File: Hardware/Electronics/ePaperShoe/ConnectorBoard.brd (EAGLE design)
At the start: 19.3 x 19.2 mm, 3 parts, among them X1 FH12-26S-0.5SH, X2 FH12-26S-0.5SH

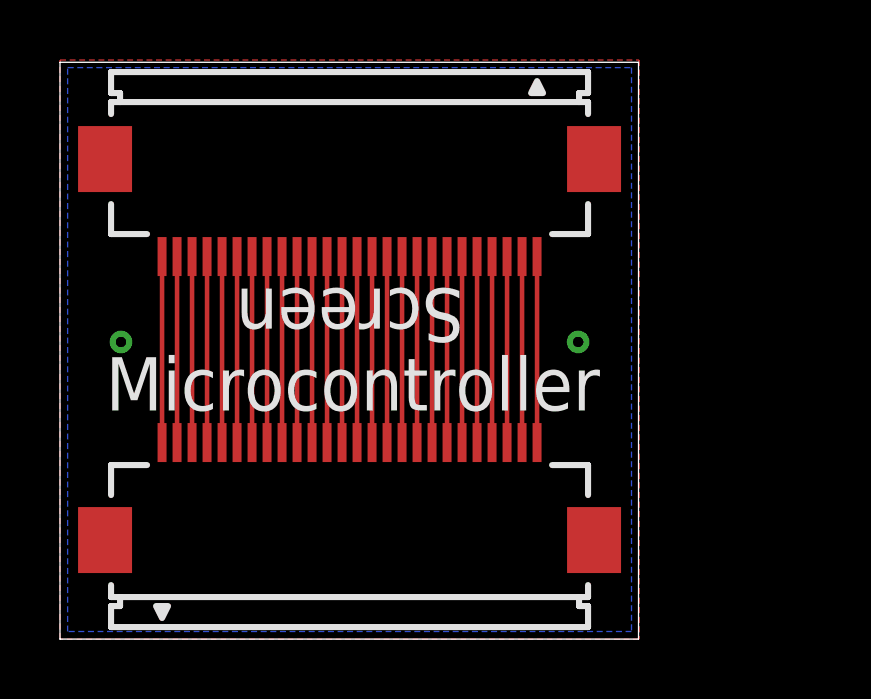
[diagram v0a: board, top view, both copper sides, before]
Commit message: Designed new screen board and made minor changes to the connector board
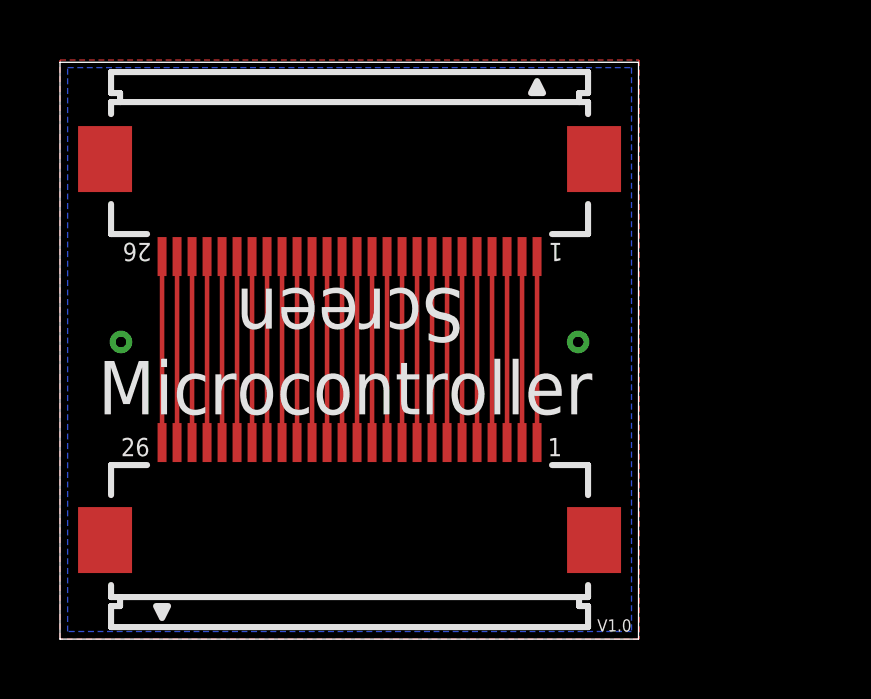
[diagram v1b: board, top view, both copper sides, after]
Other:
- board text added: "1"
- board text added: "26"
- board text added: "V1.0"
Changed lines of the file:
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@@
 <setting verticaltext="up"/>
 </settings>
-<grid distance="10" unitdist="mil" unit="mil" style="lines" multiple="1" display="no" altdistance="5" altunitdist="mil" altunit="mil"/>
+<grid distance="5" unitdist="mil" unit="mil" style="lines" multiple="1" display="no" altdistance="5" altunitdist="mil" altunit="mil"/>
 <layers>
 <layer number="1" name="Top" color="4" fill="1" visible="yes" active="yes"/>
@@
 <wire x1="19.792" y1="19.736" x2="0.508" y2="19.736" width="0" layer="20"/>
 <wire x1="0.508" y1="19.736" x2="0.508" y2="0.508" width="0" layer="20"/>
-<text x="18.034" y="2.794" size="1.778" layer="22" rot="MR0">Microcontroller</text>
-<text x="2.032" y="8.128" size="1.778" layer="21">Microcontroller</text>
+<text x="18.542" y="3.81" size="1.778" layer="22" rot="MR0" align="center-left">Microcontroller</text>
+<text x="1.778" y="8.89" size="1.778" layer="21" align="center-left">Microcontroller</text>
 <text x="13.97" y="12.192" size="1.778" layer="21" rot="SR180">Screen</text>
 <text x="6.35" y="17.526" size="1.778" layer="22" rot="SMR180">Screen</text>
-<text x="1.016" y="15.24" size="0.4064" layer="22" rot="SR270">Made for Bioworld ePaper Screen Project</text>
-<text x="19.558" y="8.636" size="0.4064" layer="22" rot="SR90">Michael Currie</text>
+<text x="19.558" y="19.304" size="0.4064" layer="22" rot="SMR270">Made for Bioworld ePaper Screen Project</text>
+<text x="19.558" y="4.572" size="0.4064" layer="22" rot="SMR270">Michael Currie</text>
+<text x="18.415" y="0.762" size="0.4064" layer="21" rot="SR0">V1.0</text>
+<text x="16.764" y="6.604" size="0.6096" layer="21">1</text>
+<text x="17.272" y="13.716" size="0.6096" layer="21" rot="SR180">1</text>
+<text x="3.556" y="13.716" size="0.6096" layer="21" rot="SR180">26</text>
+<text x="2.54" y="6.604" size="0.6096" layer="21">26</text>
 </plain>
 <attributes>
@@
 <contactref element="X1" pad="26"/>
 <contactref element="X2" pad="1"/>
-<wire x1="16.41" y1="7.06" x2="16.41" y2="13.26" width="0.1524" layer="1"/>
-</signal>
-<signal name="N$2">
-<contactref element="X1" pad="25"/>
-<contactref element="X2" pad="2"/>
-<wire x1="15.91" y1="7.06" x2="15.91" y2="13.26" width="0.1524" layer="1"/>
-</signal>
-<signal name="N$3">
-<contactref element="X1" pad="24"/>
-<contactref element="X2" pad="3"/>
-<wire x1="15.41" y1="7.06" x2="15.41" y2="13.26" width="0.1524" layer="1"/>
-</signal>
-<signal name="N$4">
-<contactref element="X1" pad="23"/>
-<contactref element="X2" pad="4"/>
-<wire x1="14.91" y1="7.06" x2="14.91" y2="13.26" width="0.1524" layer="1"/>
+<wire x1="16.41" y1="13.26" x2="16.41" y2="7.06" width="0.1524" layer="1"/>
 </signal>
 <signal name="N$5">
@@
 <wire x1="13.41" y1="7.06" x2="13.41" y2="13.26" width="0.1524" layer="1"/>
 </signal>
-<signal name="N$8">
-<contactref element="X1" pad="19"/>
-<contactref element="X2" pad="8"/>
-<wire x1="12.91" y1="7.06" x2="12.91" y2="13.26" width="0.1524" layer="1"/>
-</signal>
-<signal name="N$9">
-<contactref element="X1" pad="18"/>
-<contactref element="X2" pad="9"/>
-<wire x1="12.41" y1="7.06" x2="12.41" y2="13.26" width="0.1524" layer="1"/>
-</signal>
 <signal name="N$10">
 <contactref element="X1" pad="17"/>
@@
 <wire x1="7.91" y1="7.06" x2="7.91" y2="13.26" width="0.1524" layer="1"/>
 </signal>
-<signal name="N$19">
-<contactref element="X1" pad="8"/>
-<contactref element="X2" pad="19"/>
-<wire x1="7.41" y1="7.06" x2="7.41" y2="13.26" width="0.1524" layer="1"/>
-</signal>
 <signal name="N$20">
 <contactref element="X1" pad="7"/>
@@
 <contactref element="X2" pad="22"/>
 <wire x1="5.91" y1="7.06" x2="5.91" y2="13.26" width="0.1524" layer="1"/>
-</signal>
-<signal name="N$23">
-<contactref element="X1" pad="4"/>
-<contactref element="X2" pad="23"/>
-<wire x1="5.41" y1="7.06" x2="5.41" y2="13.26" width="0.1524" layer="1"/>
-</signal>
-<signal name="N$24">
-<contactref element="X1" pad="3"/>
-<contactref element="X2" pad="24"/>
-<wire x1="4.91" y1="7.06" x2="4.91" y2="13.26" width="0.1524" layer="1"/>
-</signal>
-<signal name="N$25">
-<contactref element="X1" pad="2"/>
-<contactref element="X2" pad="25"/>
-<wire x1="4.41" y1="7.06" x2="4.41" y2="13.26" width="0.1524" layer="1"/>
 </signal>
 <signal name="N$26">
@@
 <via x="17.78" y="10.414" extent="1-16" drill="0.35"/>
 <via x="2.54" y="10.414" extent="1-16" drill="0.35"/>
-<wire x1="17.78" y1="10.414" x2="2.54" y2="10.414" width="0" layer="19" extent="1-1"/>
+</signal>
+<signal name="N$19">
+<contactref element="X2" pad="25"/>
+<contactref element="X1" pad="2"/>
+<wire x1="4.41" y1="13.26" x2="4.41" y2="7.06" width="0.1524" layer="1"/>
+</signal>
+<signal name="N$23">
+<contactref element="X2" pad="24"/>
+<contactref element="X1" pad="3"/>
+<wire x1="4.91" y1="13.26" x2="4.91" y2="7.06" width="0.1524" layer="1"/>
+</signal>
+<signal name="N$24">
+<contactref element="X2" pad="23"/>
+<contactref element="X1" pad="4"/>
+<wire x1="5.41" y1="13.26" x2="5.41" y2="7.06" width="0.1524" layer="1"/>
+</signal>
+<signal name="N$25">
+<contactref element="X2" pad="19"/>
+<contactref element="X1" pad="8"/>
+<wire x1="7.41" y1="13.26" x2="7.41" y2="7.06" width="0.1524" layer="1"/>
+</signal>
+<signal name="N$2">
+<contactref element="X2" pad="9"/>
+<contactref element="X1" pad="18"/>
+<wire x1="12.41" y1="13.26" x2="12.41" y2="7.06" width="0.1524" layer="1"/>
+</signal>
+<signal name="N$3">
+<contactref element="X2" pad="4"/>
+<contactref element="X1" pad="23"/>
+<wire x1="14.91" y1="13.26" x2="14.91" y2="7.06" width="0.1524" layer="1"/>
+</signal>
+<signal name="N$4">
+<contactref element="X2" pad="3"/>
+<contactref element="X1" pad="24"/>
+<wire x1="15.41" y1="13.26" x2="15.41" y2="7.06" width="0.1524" layer="1"/>
+</signal>
+<signal name="N$8">
+<contactref element="X2" pad="2"/>
+<contactref element="X1" pad="25"/>
+<wire x1="15.91" y1="13.26" x2="15.91" y2="7.06" width="0.1524" layer="1"/>
+</signal>
+<signal name="N$9">
+<contactref element="X2" pad="8"/>
+<contactref element="X1" pad="19"/>
+<wire x1="12.91" y1="13.26" x2="12.91" y2="7.06" width="0.1524" layer="1"/>
 </signal>
 </signals>
